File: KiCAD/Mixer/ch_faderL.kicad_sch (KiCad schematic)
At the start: 4 parts, among them U4 NE5532

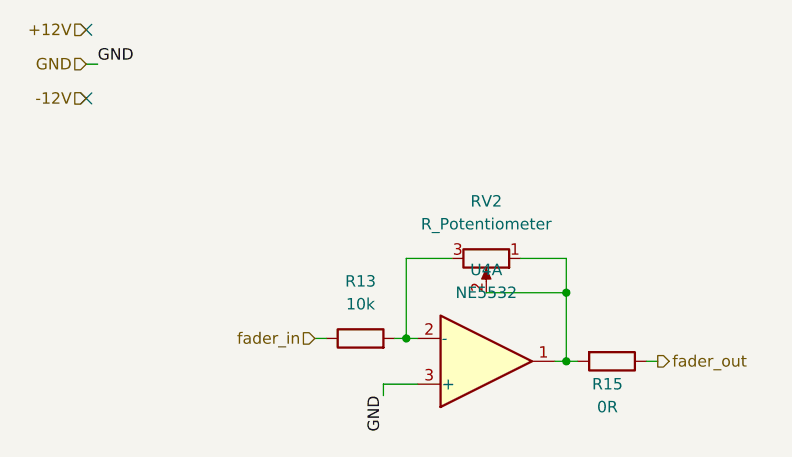
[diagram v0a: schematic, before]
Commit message: Rework of schematic, with error fixes and reworked pcb
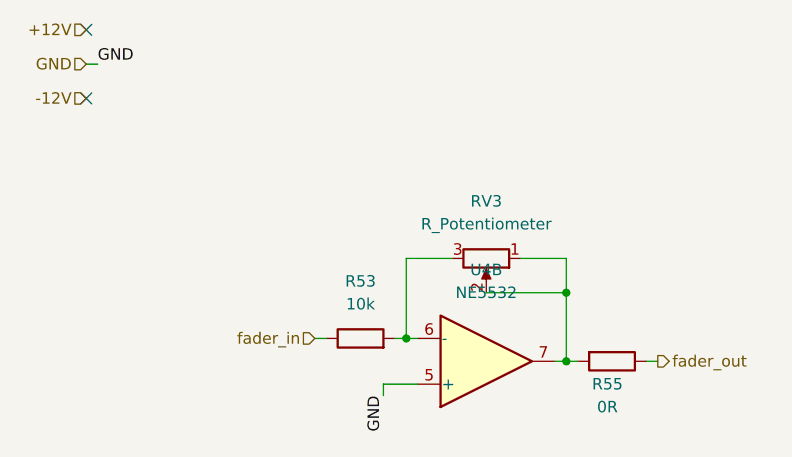
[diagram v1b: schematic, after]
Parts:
- removed RV2: R_Potentiometer, Potentiometer_THT:Potentiometer_Bourns_PTA4543_Single_Slide, symbol Device:R_Potentiometer
- removed U4: NE5532, Package_SO:SOIC-8_3.9x4.9mm_P1.27mm, symbol Amplifier_Operational:NE5532
- added RV3: R_Potentiometer, Potentiometer_THT:Potentiometer_Bourns_PTA4543_Single_Slide, symbol Device:R_Potentiometer
- added U4: NE5532, Package_SO:SOIC-8_3.9x4.9mm_P1.27mm, symbol Amplifier_Operational:NE5532
- renumbered R13 to R53, R15 to R55
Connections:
- net GND: now also U4.5 (+)
- net at R55.2: now also RV3.1, RV3.2, U4.7
- net at R53.2: now also RV3.3, U4.6 (-)

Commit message: Final PCB Version that got ordered from JLCPCB
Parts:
- removed R53: 10k, Resistor_SMD:R_0805_2012Metric_Pad1.20x1.40mm_HandSolder, symbol Device:R
- added R56: 0R, Resistor_SMD:R_0805_2012Metric_Pad1.20x1.40mm_HandSolder, symbol Device:R
- R55: value 0R -> 10k
- renumbered RV3 to RV8, U4 to U2
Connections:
- net fader_in: now also R55.1
- net fader_out: now also R56.1; no longer R55.1
- net at RV8.3, U2.6 (-): now also R55.2
- net at RV8.1, RV8.2, U2.7: now also R56.2; no longer R55.2
